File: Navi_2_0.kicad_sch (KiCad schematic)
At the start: 98 parts, among them J1 USB_B_Micro, J10 BAT-, J2 Conn_01x24_Male, J27 Micro_SD_Card_Det, J9 BAT+, Q1 DMG2301L-7, Q2 TF2310, Q3 DMG2301L-7, Q4 Q_NPN_BEC, Q5 Q_NPN_BEC, Q6 DMG2301L-7, Q7 DMG2301L-7, SW1 SW_Push, SW2 SW_Push, U1 MT3420C, U2 MT3420C, U3 ESP32-WROOM-32, U4 CH340K, U5 L96-M33, U6 LSM303AH, U7 TCN75-3.3

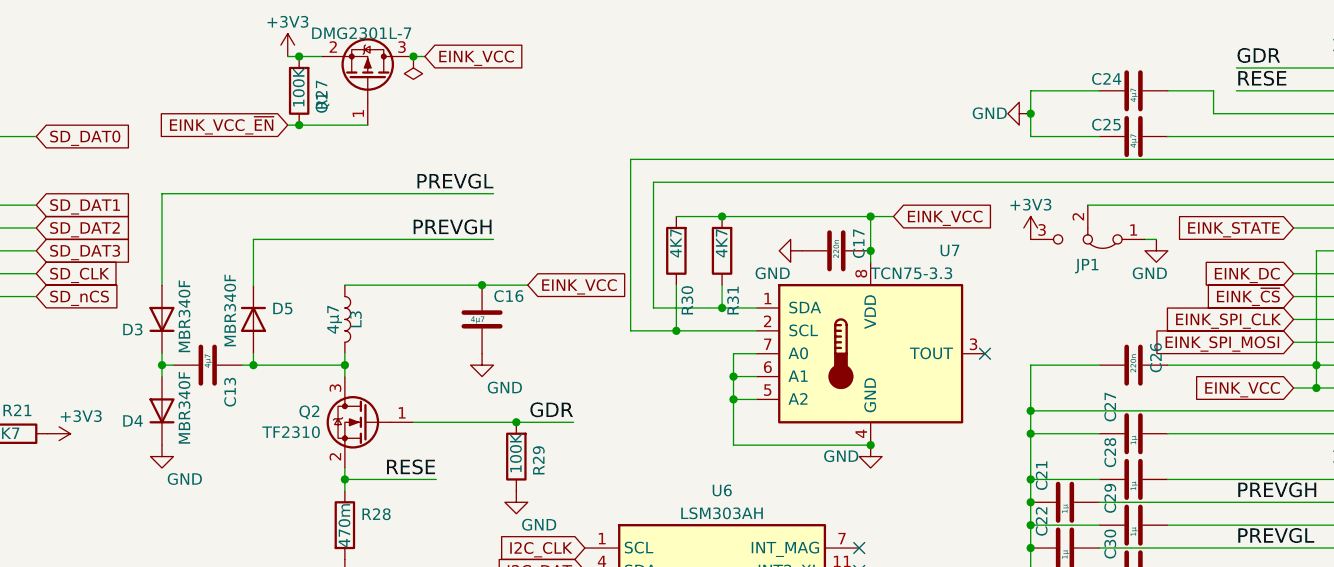
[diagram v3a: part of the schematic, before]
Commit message: Layout V3 erster Wurf
Layout V3 vor DRC
(Siebdruck und Leiterbahnen fertig)
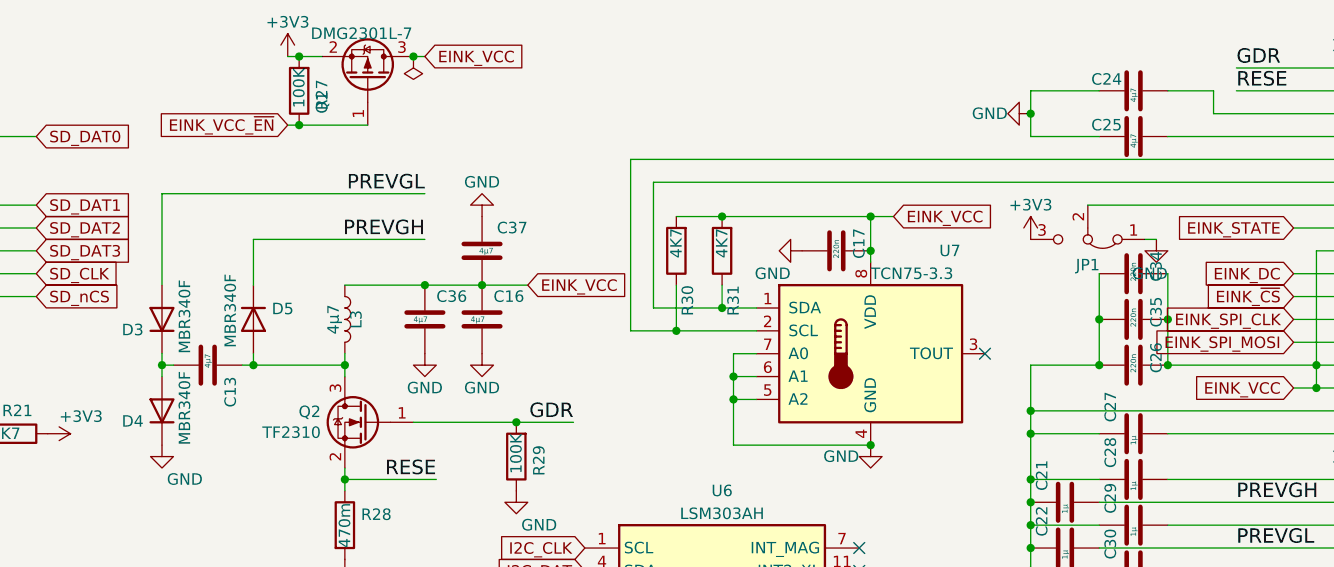
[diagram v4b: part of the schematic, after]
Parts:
- added C34, C35: 220n, Capacitor_SMD:C_0603_1608Metric, symbol Device:C
- added C36, C37: 4µ7, Capacitor_SMD:C_0603_1608Metric, symbol Device:C
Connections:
- net EINK_VCC: now also C34.1, C35.1, C36.1, C37.1
- net GND: now also C34.2, C35.2, C36.2, C37.2
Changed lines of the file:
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@@
   (junction (at 154.94 66.04) (diameter 0.9144) (color 0 0 0 0))
   (junction (at 162.56 19.05) (diameter 0.9144) (color 0 0 0 0))
+  (junction (at 163.83 44.45) (diameter 0.9144) (color 0 0 0 0))
   (junction (at 163.83 147.32) (diameter 0.9144) (color 0 0 0 0))
   (junction (at 163.83 149.86) (diameter 0.9144) (color 0 0 0 0))
@@
   (junction (at 236.22 91.44) (diameter 0.9144) (color 0 0 0 0))
   (junction (at 236.22 102.87) (diameter 0.9144) (color 0 0 0 0))
+  (junction (at 238.76 48.26) (diameter 0.9144) (color 0 0 0 0))
+  (junction (at 238.76 53.34) (diameter 0.9144) (color 0 0 0 0))
   (junction (at 243.84 91.44) (diameter 0.9144) (color 0 0 0 0))
+  (junction (at 246.38 48.26) (diameter 0.9144) (color 0 0 0 0))
+  (junction (at 246.38 53.34) (diameter 0.9144) (color 0 0 0 0))
   (junction (at 252.73 91.44) (diameter 0.9144) (color 0 0 0 0))
   (junction (at 255.27 91.44) (diameter 0.9144) (color 0 0 0 0))
@@
     (stroke (width 0) (type solid) (color 0 0 0 0))
   )
-  (wire (pts (xy 134.62 34.29) (xy 171.45 34.29))
+  (wire (pts (xy 134.62 34.29) (xy 163.83 34.29))
     (stroke (width 0) (type solid) (color 0 0 0 0))
   )
@@
     (stroke (width 0) (type solid) (color 0 0 0 0))
   )
-  (wire (pts (xy 144.78 39.37) (xy 171.45 39.37))
+  (wire (pts (xy 144.78 39.37) (xy 163.83 39.37))
     (stroke (width 0) (type solid) (color 0 0 0 0))
   )
@@
     (stroke (width 0) (type solid) (color 0 0 0 0))
   )
+  (wire (pts (xy 163.83 44.45) (xy 154.94 44.45))
+    (stroke (width 0) (type solid) (color 0 0 0 0))
+  )
   (wire (pts (xy 163.83 147.32) (xy 163.83 149.86))
     (stroke (width 0) (type solid) (color 0 0 0 0))
@@
     (stroke (width 0) (type solid) (color 0 0 0 0))
   )
-  (wire (pts (xy 170.18 44.45) (xy 154.94 44.45))
+  (wire (pts (xy 170.18 44.45) (xy 163.83 44.45))
     (stroke (width 0) (type solid) (color 0 0 0 0))
   )
@@
     (stroke (width 0) (type solid) (color 0 0 0 0))
   )
+  (wire (pts (xy 238.76 43.18) (xy 238.76 48.26))
+    (stroke (width 0) (type solid) (color 0 0 0 0))
+  )
+  (wire (pts (xy 238.76 48.26) (xy 238.76 53.34))
+    (stroke (width 0) (type solid) (color 0 0 0 0))
+  )
   (wire (pts (xy 238.76 53.34) (xy 231.14 53.34))
     (stroke (width 0) (type solid) (color 0 0 0 0))
@@
     (stroke (width 0) (type solid) (color 0 0 0 0))
   )
+  (wire (pts (xy 246.38 43.18) (xy 246.38 48.26))
+    (stroke (width 0) (type solid) (color 0 0 0 0))
+  )
+  (wire (pts (xy 246.38 48.26) (xy 246.38 53.34))
+    (stroke (width 0) (type solid) (color 0 0 0 0))
+  )
   (wire (pts (xy 246.38 53.34) (xy 262.89 53.34))
     (stroke (width 0) (type solid) (color 0 0 0 0))
@@
     (effects (font (size 1.27 1.27)) (justify left bottom))
   )
-  (label "RESE" (at 165.1 66.04 180)
+  (label "PREVGL" (at 163.83 34.29 180)
     (effects (font (size 1.6002 1.6002)) (justify right bottom))
   )
-  (label "PREVGL" (at 171.45 34.29 180)
+  (label "PREVGH" (at 163.83 39.37 180)
     (effects (font (size 1.6002 1.6002)) (justify right bottom))
   )
-  (label "PREVGH" (at 171.45 39.37 180)
+  (label "RESE" (at 165.1 66.04 180)
     (effects (font (size 1.6002 1.6002)) (justify right bottom))
   )
@@
     (pin "1")
   )
+  (symbol (lib_id "power:GND") (at 163.83 52.07 0) (unit 1)
+    (in_bom yes) (on_board yes)
+    (property "Reference" "#PWR020" (id 0) (at 163.83 58.42 0)
+      (effects (font (size 1.27 1.27)) hide)
+    )
+    (property "Value" "GND" (id 1) (at 163.83 55.88 0))
+    (property "Footprint" "" (id 2) (at 163.83 52.07 0)
+      (effects (font (size 1.27 1.27)) hide)
+    )
+    (property "Datasheet" "" (id 3) (at 163.83 52.07 0)
+      (effects (font (size 1.27 1.27)) hide)
+    )
+    (pin "1")
+  )
   (symbol (lib_id "power:GND") (at 165.1 190.5 0) (unit 1)
     (in_bom yes) (on_board yes)
@@
     (pin "1")
   )
+  (symbol (lib_id "power:GND") (at 170.18 36.83 180) (unit 1)
+    (in_bom yes) (on_board yes)
+    (property "Reference" "#PWR021" (id 0) (at 170.18 30.48 0)
+      (effects (font (size 1.27 1.27)) hide)
+    )
+    (property "Value" "GND" (id 1) (at 170.18 33.02 0))
+    (property "Footprint" "" (id 2) (at 170.18 36.83 0)
+      (effects (font (size 1.27 1.27)) hide)
+    )
+    (property "Datasheet" "" (id 3) (at 170.18 36.83 0)
+      (effects (font (size 1.27 1.27)) hide)
+    )
+    (pin "1")
+  )
   (symbol (lib_id "power:GND") (at 170.18 52.07 0) (unit 1)
     (in_bom yes) (on_board yes)
@@
       (effects (font (size 1.27 1.27)) hide)
     )
-    (property "Value" "GND" (id 1) (at 172.72 55.88 0))
+    (property "Value" "GND" (id 1) (at 170.18 55.88 0))
     (property "Footprint" "" (id 2) (at 170.18 52.07 0)
       (effects (font (size 1.27 1.27)) hide)
@@
     (pin "2")
   )
+  (symbol (lib_id "Device:C") (at 163.83 48.26 0) (unit 1)
+    (in_bom yes) (on_board yes)
+    (property "Reference" "C36" (id 0) (at 165.1 45.72 0)
+      (effects (font (size 1.27 1.27)) (justify left))
+    )
+    (property "Value" "4µ7" (id 1) (at 162.56 48.26 0)
+      (effects (font (size 0.6096 0.6096)) (justify left))
+    )
+    (property "Footprint" "Capacitor_SMD:C_0603_1608Metric" (id 2) (at 164.7952 52.07 0)
+      (effects (font (size 1.27 1.27)) hide)
+    )
+    (property "Datasheet" "~" (id 3) (at 163.83 48.26 0)
+      (effects (font (size 1.27 1.27)) hide)
+    )
+    (property "LCSC" "C307468" (id 4) (at 163.83 48.26 0)
+      (effects (font (size 1.27 1.27)) hide)
+    )
+    (pin "1")
+    (pin "2")
+  )
   (symbol (lib_id "Device:C") (at 166.37 156.21 0) (unit 1)
     (in_bom yes) (on_board yes)
@@
     (pin "2")
   )
+  (symbol (lib_id "Device:C") (at 170.18 40.64 180) (unit 1)
+    (in_bom yes) (on_board yes)
+    (property "Reference" "C37" (id 0) (at 175.26 38.1 0)
+      (effects (font (size 1.27 1.27)) (justify left))
+    )
+    (property "Value" "4µ7" (id 1) (at 171.45 40.64 0)
+      (effects (font (size 0.6096 0.6096)) (justify left))
+    )
+    (property "Footprint" "Capacitor_SMD:C_0603_1608Metric" (id 2) (at 169.2148 36.83 0)
+      (effects (font (size 1.27 1.27)) hide)
+    )
+    (property "Datasheet" "~" (id 3) (at 170.18 40.64 0)
+      (effects (font (size 1.27 1.27)) hide)
+    )
+    (property "LCSC" "C307468" (id 4) (at 170.18 40.64 0)
+      (effects (font (size 1.27 1.27)) hide)
+    )
+    (pin "1")
+    (pin "2")
+  )
   (symbol (lib_id "Device:C") (at 170.18 48.26 0) (unit 1)
     (in_bom yes) (on_board yes)
@@
     (pin "2")
   )
+  (symbol (lib_id "Device:C") (at 242.57 43.18 270) (unit 1)
+    (in_bom yes) (on_board yes)
+    (property "Reference" "C34" (id 0) (at 245.11 40.64 0)
+      (effects (font (size 1.27 1.27)) (justify left))
+    )
+    (property "Value" "220n" (id 1) (at 242.57 41.91 0)
+      (effects (font (size 0.6096 0.6096)) (justify left))
+    )
+    (property "Footprint" "Capacitor_SMD:C_0603_1608Metric" (id 2) (at 238.76 44.1452 0)
+      (effects (font (size 1.27 1.27)) hide)
+    )
+    (property "Datasheet" "~" (id 3) (at 242.57 43.18 0)
+      (effects (font (size 1.27 1.27)) hide)
+    )
+    (property "LCSC" "C163696" (id 4) (at 242.57 43.18 0)
+      (effects (font (size 1.27 1.27)) hide)
+    )
+    (pin "1")
+    (pin "2")
+  )
+  (symbol (lib_id "Device:C") (at 242.57 48.26 270) (unit 1)
+    (in_bom yes) (on_board yes)
+    (property "Reference" "C35" (id 0) (at 245.11 45.72 0)
+      (effects (font (size 1.27 1.27)) (justify left))
+    )
+    (property "Value" "220n" (id 1) (at 242.57 46.99 0)
+      (effects (font (size 0.6096 0.6096)) (justify left))
+    )
+    (property "Footprint" "Capacitor_SMD:C_0603_1608Metric" (id 2) (at 238.76 49.2252 0)
+      (effects (font (size 1.27 1.27)) hide)
+    )
+    (property "Datasheet" "~" (id 3) (at 242.57 48.26 0)
+      (effects (font (size 1.27 1.27)) hide)
+    )
+    (property "LCSC" "C163696" (id 4) (at 242.57 48.26 0)
+      (effects (font (size 1.27 1.27)) hide)
+    )
+    (pin "1")
+    (pin "2")
+  )
   (symbol (lib_id "Device:C") (at 242.57 53.34 270) (unit 1)
     (in_bom yes) (on_board yes)
@@
       (reference "#PWR019") (unit 1) (value "GND") (footprint "")
     )
+    (path "/a82c4c34-4e5b-4388-b8e5-6b425bd49338"
+      (reference "#PWR020") (unit 1) (value "GND") (footprint "")
+    )
+    (path "/ea560508-5125-4430-9fdf-2d9d520351f4"
+      (reference "#PWR021") (unit 1) (value "GND") (footprint "")
+    )
     (path "/00000000-0000-0000-0000-00005fd87118"
       (reference "#PWR031") (unit 1) (value "+BATT") (footprint "")
@@
       (reference "C33") (unit 1) (value "4µ7") (footprint "Capacitor_SMD:C_0603_1608Metric")
     )
+    (path "/8ba762da-b091-479d-9800-53e247adece3"
+      (reference "C34") (unit 1) (value "220n") (footprint "Capacitor_SMD:C_0603_1608Metric")
+    )
+    (path "/b27f67dd-948e-479d-b510-8bc6b6570ac0"
+      (reference "C35") (unit 1) (value "220n") (footprint "Capacitor_SMD:C_0603_1608Metric")
+    )
+    (path "/938c84eb-4ba9-4cad-a4f6-63e7578fb26f"
+      (reference "C36") (unit 1) (value "4µ7") (footprint "Capacitor_SMD:C_0603_1608Metric")
+    )
+    (path "/02a2f3a0-948e-424c-8748-45116c8e2013"
+      (reference "C37") (unit 1) (value "4µ7") (footprint "Capacitor_SMD:C_0603_1608Metric")
+    )
     (path "/00000000-0000-0000-0000-0000605ba9c6"
